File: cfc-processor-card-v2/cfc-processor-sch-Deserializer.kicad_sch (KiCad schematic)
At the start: 25 parts, among them U13 DS90CR218AMTD/NOPB

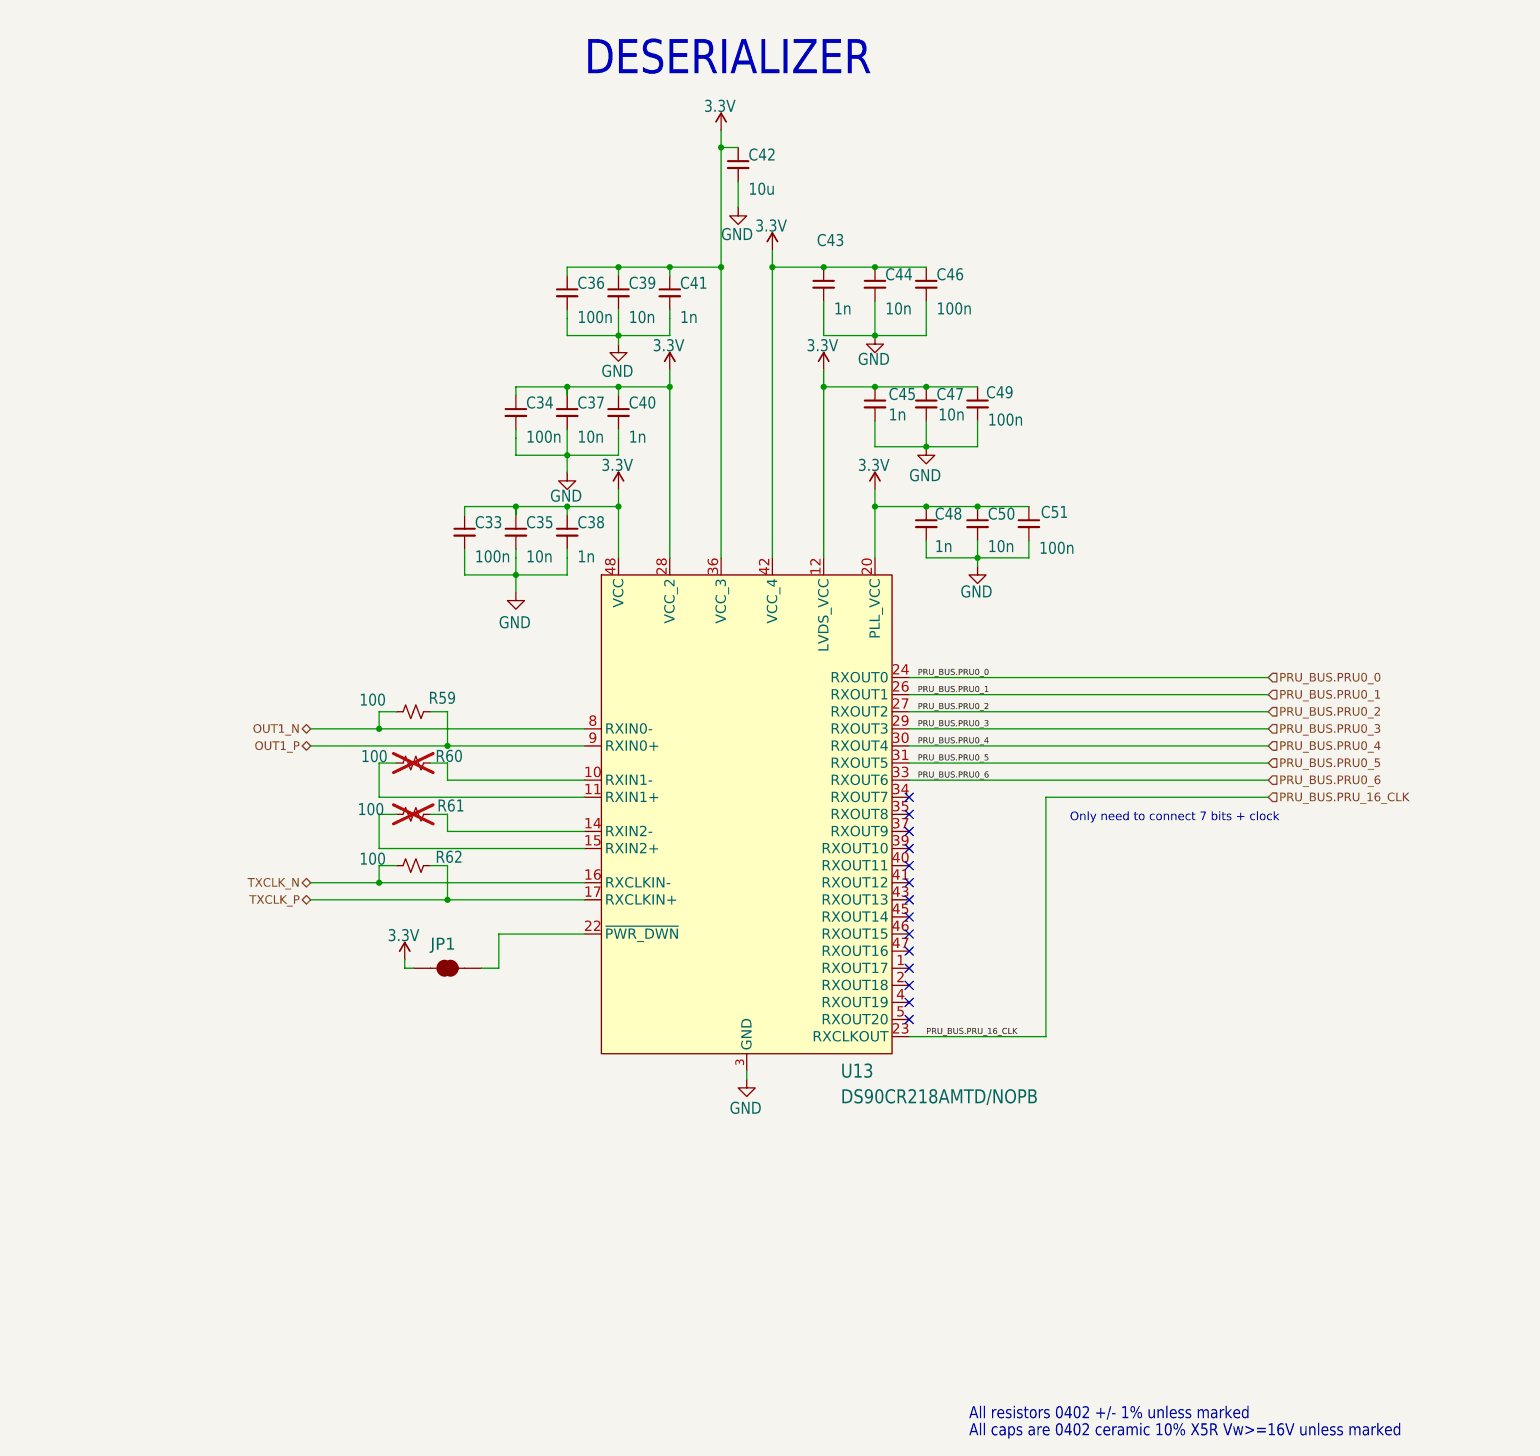
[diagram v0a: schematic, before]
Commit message: Updated OPD
couple of resistors and caps added to schematic. Changed USB ESD clamp VDD to 3.3v instead of octavo created VDD line.
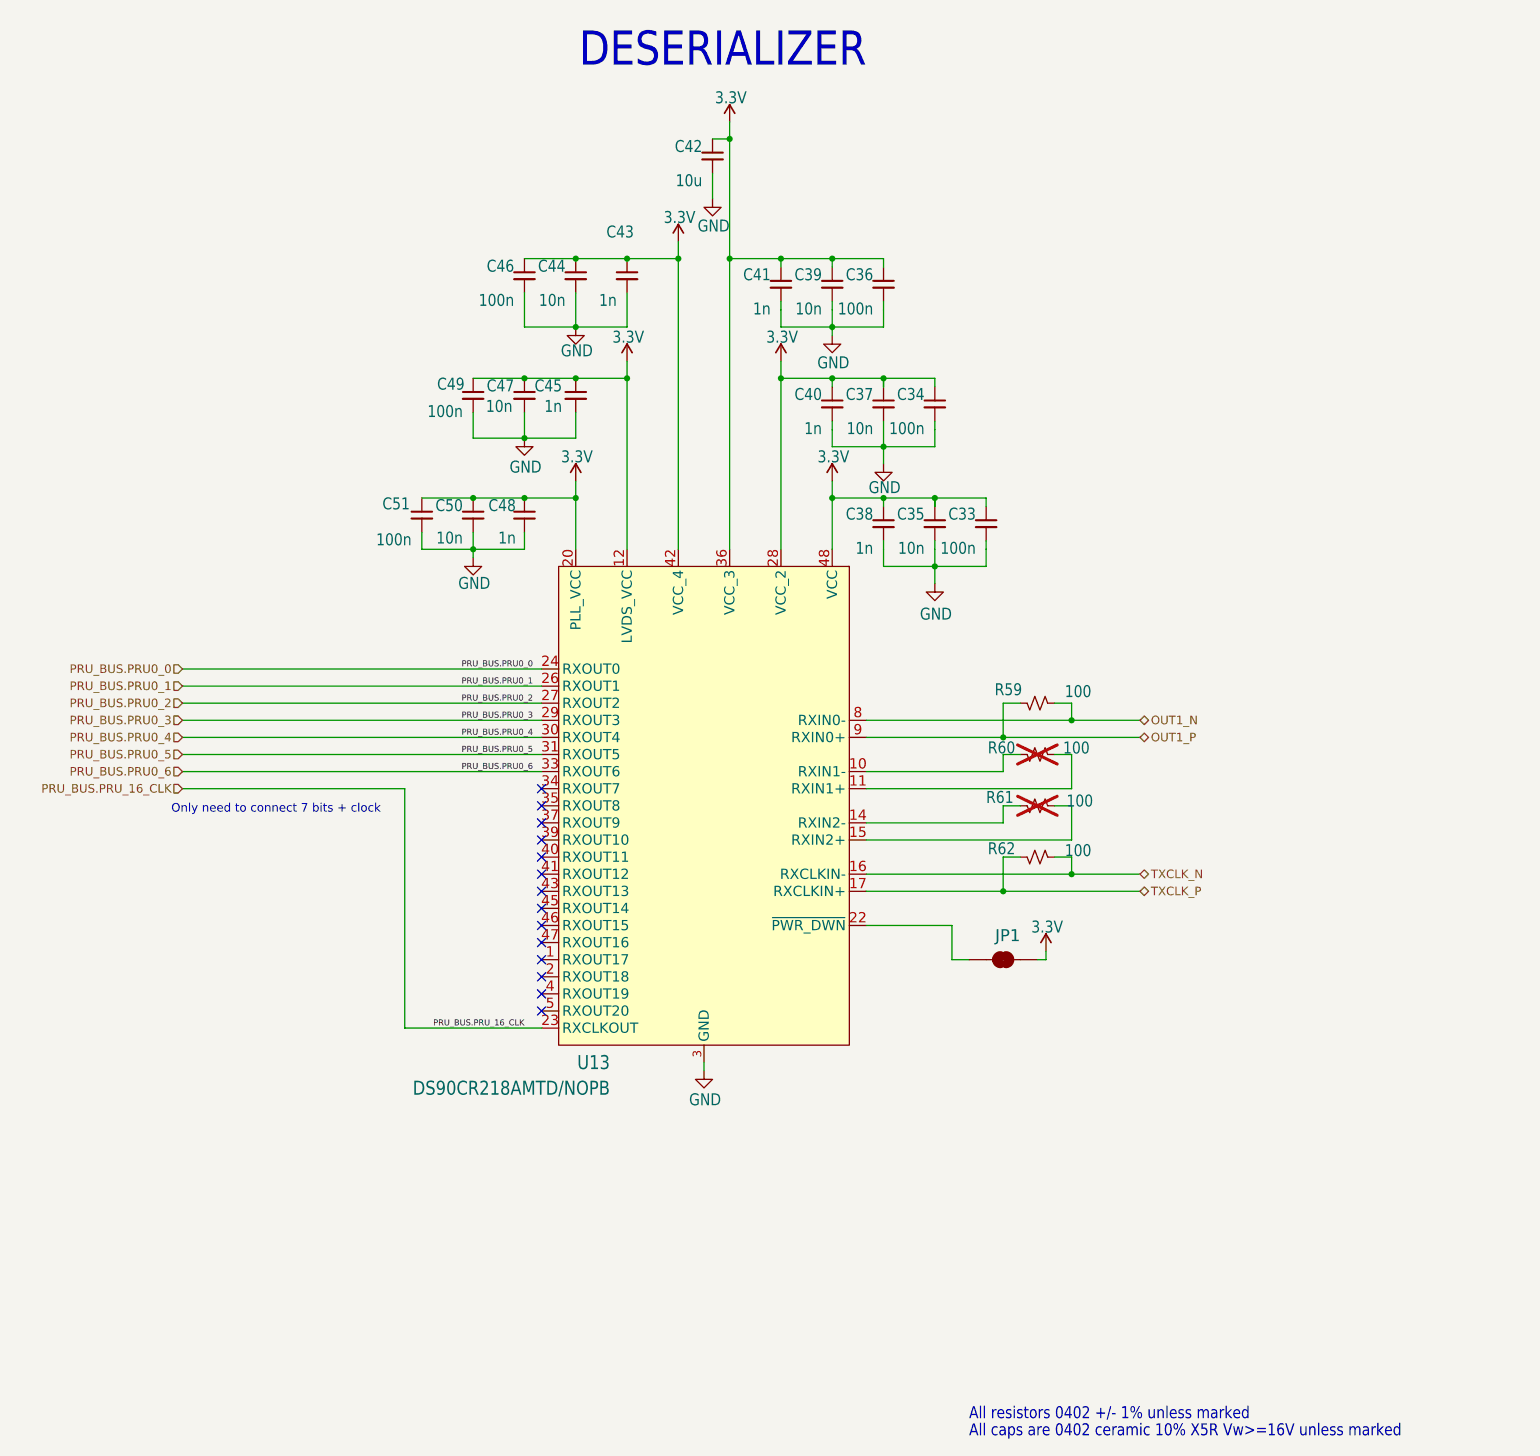
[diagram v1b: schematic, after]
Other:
- moved on the sheet: C33, C34, C35, C36, C37, C38, C39, C40, C41, C42, C43, C44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

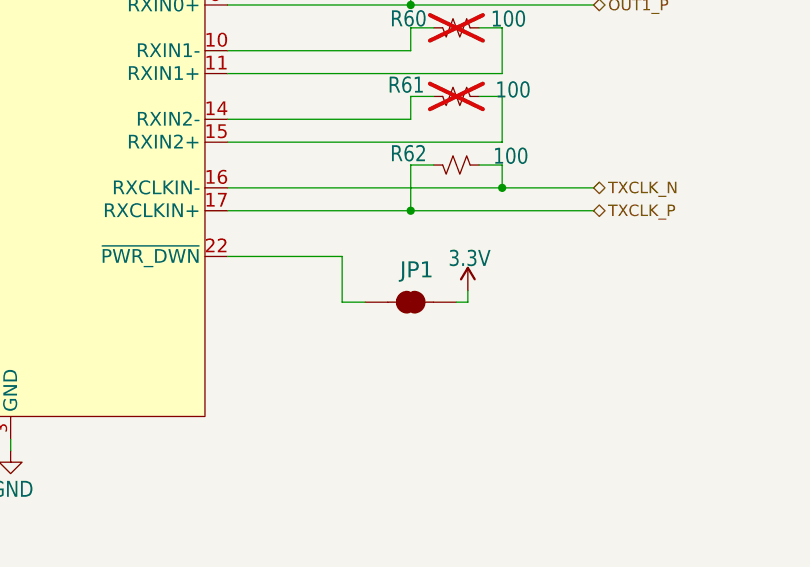
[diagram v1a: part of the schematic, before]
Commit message: Update
Fixed a couple of library issues on testpoints and other misc components. Added Pull up resistors to 8 channel i2c ic
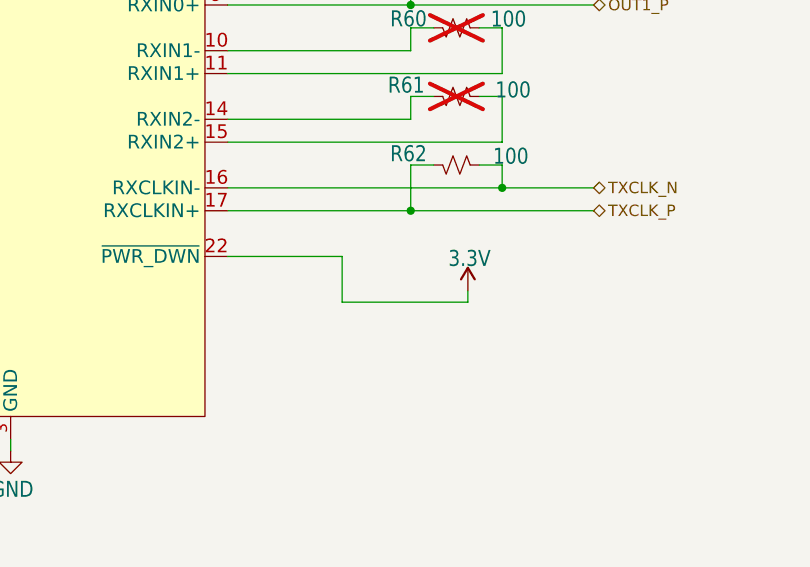
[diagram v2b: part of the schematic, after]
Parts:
- removed JP1: JUMPER-SMT_2_NC_TRACE_SILK, cfc-card:SMT-JUMPER_2_NC_TRACE_SILK, symbol cfc-card-eagle-import:JUMPER-SMT_2_NC_TRACE_SILK
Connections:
- net 3.3V: now also U13.22 (~{PWR_DWN})
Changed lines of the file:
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@@
 	(wire
 		(pts
-			(xy 243.84 191.77) (xy 241.3 191.77)
+			(xy 241.3 191.77) (xy 255.27 191.77)
 		)
 		(stroke
@@
 	(wire
 		(pts
-			(xy 255.27 191.77) (xy 254 191.77)
-		)
-		(stroke
-			(width 0.1524)
-			(type solid)
-		)
-	)
-	(wire
-		(pts
 			(xy 160.02 201.93) (xy 180.34 201.93)
 		)
@@
 					(unit 1)
 				)
-			)
-		)
-	)
-	(symbol
-		(lib_id "cfc-card-eagle-import:JUMPER-SMT_2_NC_TRACE_SILK")
-		(at 248.92 191.77 0)
-		(mirror y)
-		(unit 1)
-		(body_style 1)
-		(exclude_from_sim no)
-		(in_bom no)
-		(on_board yes)
-		(in_pos_files yes)
-		(dnp no)
-		(property "Reference" "JP1"
-			(at 251.46 189.23 0)
-			(show_name no)
-			(do_not_autoplace no)
-			(effects
-				(font
-					(size 1.778 1.778)
-				)
-				(justify left bottom)
-			)
-		)
-		(property "Value" "JUMPER-SMT_2_NC_TRACE_SILK"
-			(at 251.46 194.31 0)
-			(hide yes)
-			(show_name no)
-			(do_not_autoplace no)
-			(effects
-				(font
-					(size 1.778 1.778)
-				)
-				(justify left top)
-			)
-		)
-		(property "Footprint" "cfc-card:SMT-JUMPER_2_NC_TRACE_SILK"
-			(at 248.92 191.77 0)
-			(hide yes)
-			(show_name no)
-			(do_not_autoplace no)
-			(effects
-				(font
-					(size 1.27 1.27)
-				)
-			)
-		)
-		(property "Datasheet" ""
-			(at 248.92 191.77 0)
-			(hide yes)
-			(show_name no)
-			(do_not_autoplace no)
-			(effects
-				(font
-					(size 1.27 1.27)
-				)
-			)
-		)
-		(property "Description" ""
-			(at 248.92 191.77 0)
-			(hide yes)
-			(show_name no)
-			(do_not_autoplace no)
-			(effects
-				(font
-					(size 1.27 1.27)
-				)
-			)
-		)
-		(pin "1"
-		)
-		(pin "2"
-		)
-		(instances
-			(project "cfc-processor"
-				(path "/07ac832f-8d98-4777-b655-1877592dfd88/fa749d49-011a-4aaa-ad4d-f74224eb48bd"
-					(reference "JP1")
-					(unit 1)
-				)
